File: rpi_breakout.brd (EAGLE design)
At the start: 36.8 x 34.3 mm, 22 parts

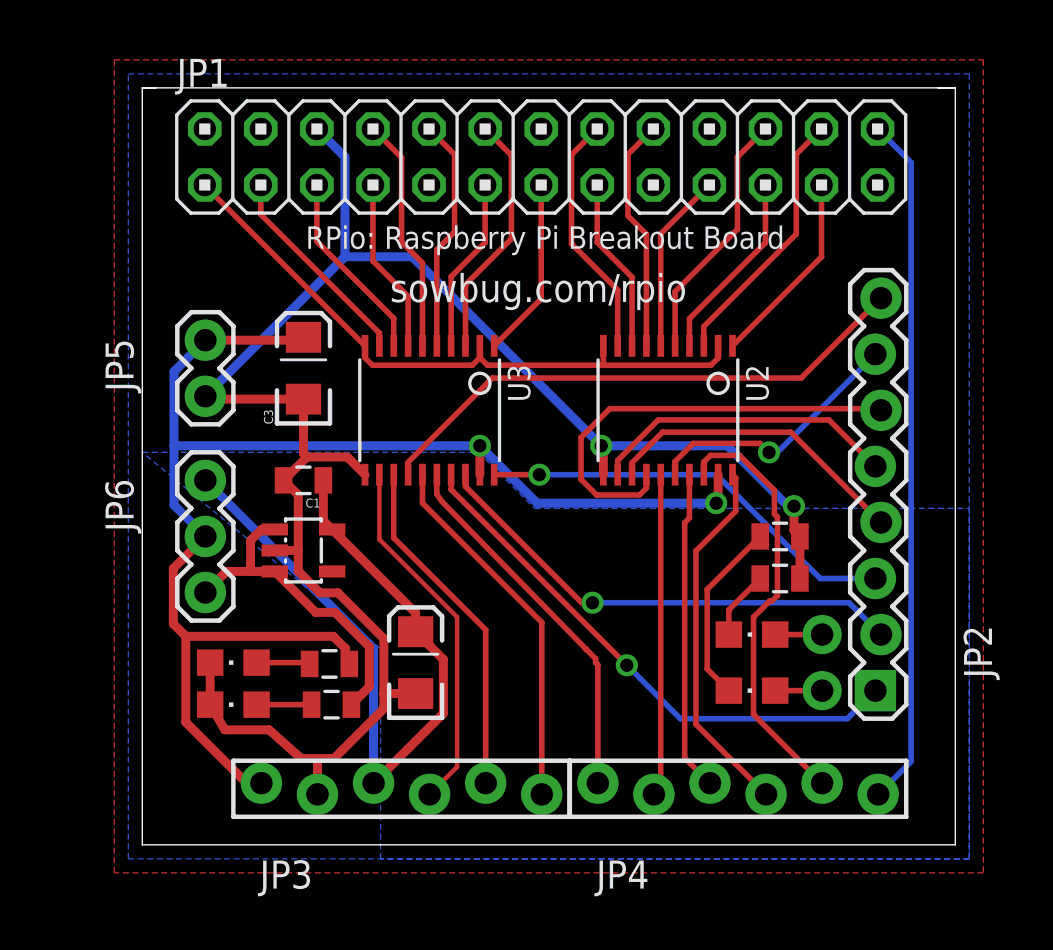
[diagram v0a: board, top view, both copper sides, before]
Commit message: Moved left IC right for shorter traces
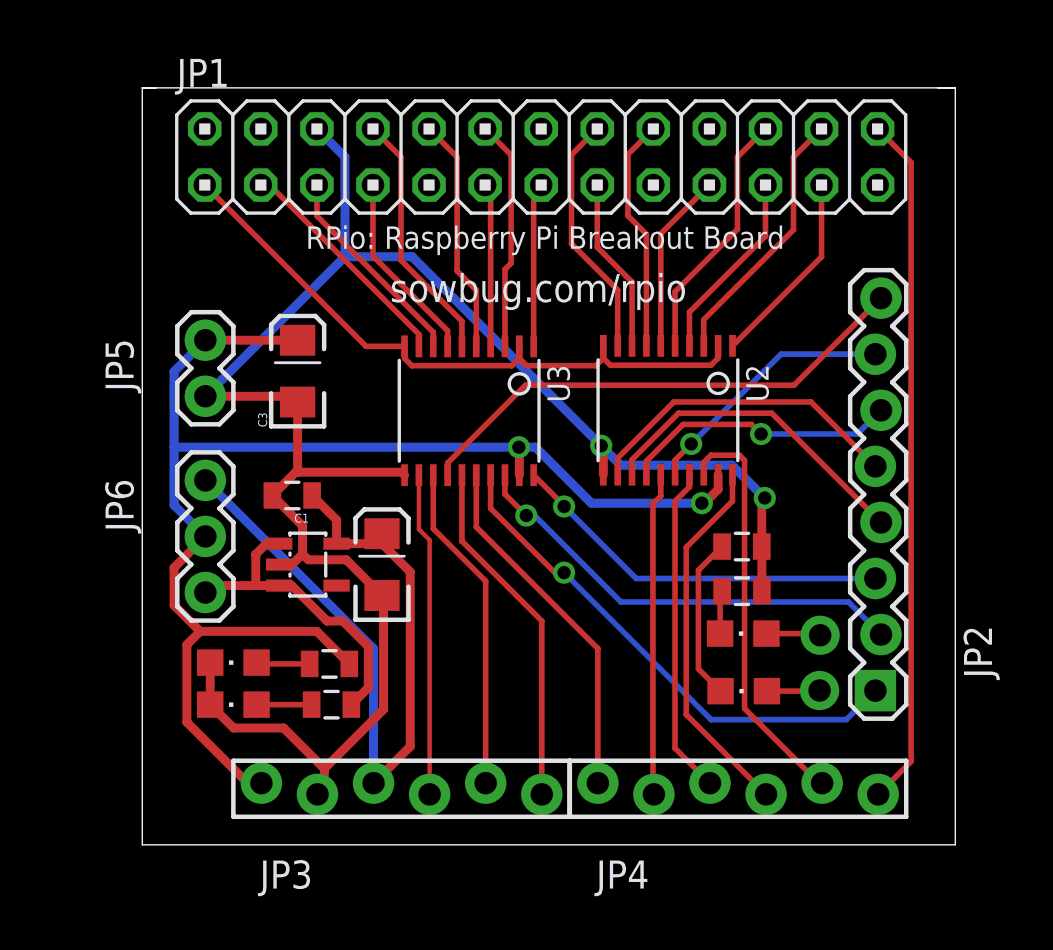
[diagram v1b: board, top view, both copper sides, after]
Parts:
- moved C2 4.69 mm to (10.2, 12.1)
- moved R3 1.82 mm to (26.5, 10.9)
- moved U3 1.79 mm to (14.2, 19.0)
- moved R4 1.79 mm to (26.5, 12.9)
- moved C1 0.85 mm to (6.16, 15.2)
- moved VREG1 0.67 mm to (6.87, 12.1)
- moved LED3 0.40 mm to (26.6, 8.93)
- moved LED4 0.38 mm to (26.6, 6.33)
- moved C3 0.30 mm to (6.40, 20.8)
- moved JP8 0.12 mm to (30.0, 6.36)
- moved JP7 0.09 mm to (30.1, 8.86)
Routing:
- net GPIOV_5: track 20.0 -> 12.6 mm, vias 0 -> 1
- net SDAV0: track 16.5 -> 14.7 mm
- net GPIOV_7: track 25.1 -> 23.3 mm
- net GPIOV_2: track 19.2 -> 17.4 mm
- net GPIOV_1: track 22.1 -> 20.5 mm
- net GPIOV_0: track 24.7 -> 23.4 mm
- net N$3: track 3.13 -> 1.96 mm
- net VCC: track 64.9 -> 63.8 mm
- net SDA0: track 9.51 -> 10.5 mm
- net N$4: track 8.39 -> 7.41 mm
- net /SPI_CEV0: track 19.7 -> 18.8 mm
- net GPIOV_3: track 14.1 -> 14.9 mm
- net TXDV: track 16.7 -> 16.0 mm
- net TXD: track 10.8 -> 11.5 mm
- net SCL0: track 8.73 -> 9.49 mm
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- removed copper zone on layer 1, net GND
- removed copper zone on layer 16, net GND
- removed copper zone on layer 16, net VCC

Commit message: Added solder jumper, RTC and diode protection, shortened traces (26.5 total)
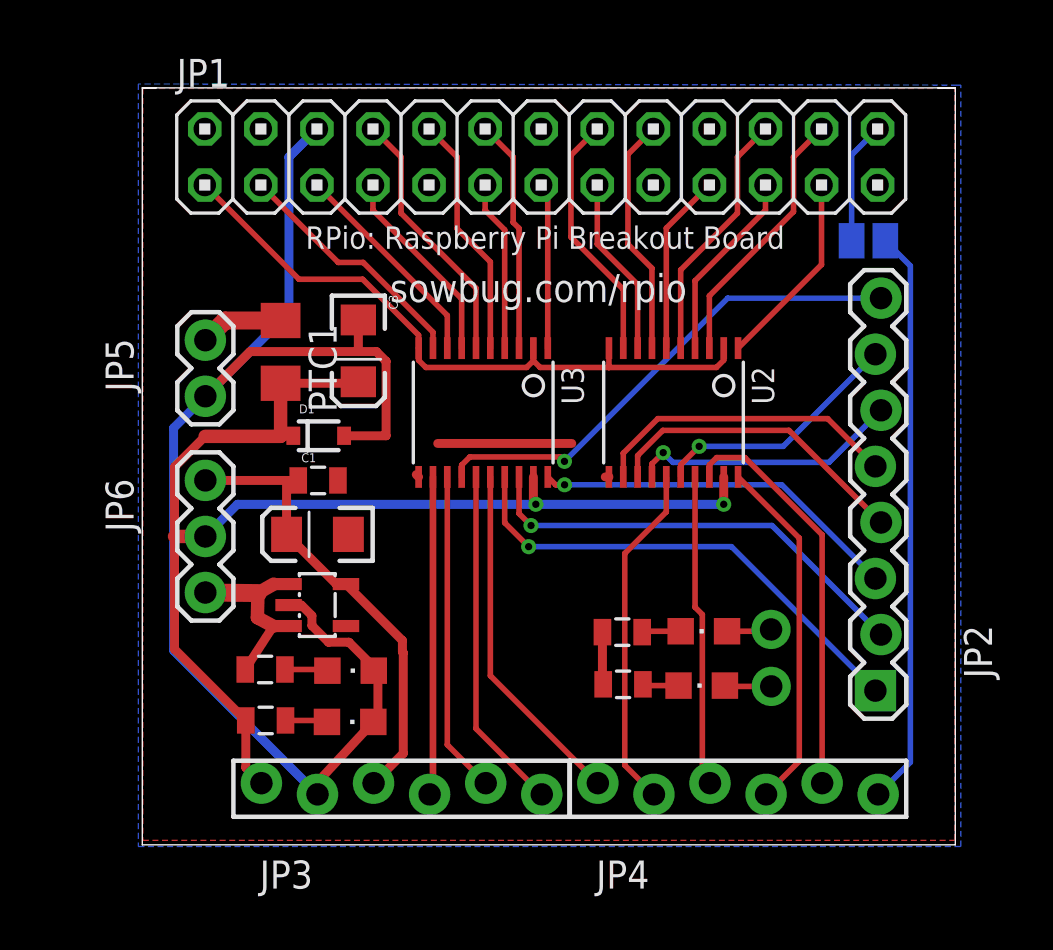
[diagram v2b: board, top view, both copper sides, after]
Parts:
- added D1: (no value), SparkFun-DiscreteSemi:SOD-323
- added PTC1: (no value), rcl:R1206
- added SJ1: SPI_CE1_3.3v_enable, jumper:SJ
- moved R4 8.24 mm to (21.1, 6.64), turned to 180 degrees
- moved LED2 5.93 mm to (8.78, 4.93), turned to 270 degrees
- moved R3 5.73 mm to (21.1, 9.00), turned to 180 degrees
- moved LED1 5.53 mm to (8.80, 7.26), turned to 270 degrees
- moved R2 3.86 mm to (4.95, 5.00), turned to 0 degrees
- moved R1 3.40 mm to (4.93, 7.31), turned to 0 degrees
- moved C2 3.23 mm to (7.30, 13.4), turned to 180 degrees
- moved C3 2.90 mm to (9.15, 21.7), turned to 270 degrees
- moved JP7 2.24 mm to (27.8, 9.12)
- moved JP8 2.20 mm to (27.9, 6.54)
- moved LED4 1.92 mm to (24.7, 6.58)
- moved VREG1 1.88 mm to (7.29, 10.2)
- moved LED3 1.79 mm to (24.8, 9.04)
- moved C1 1.35 mm to (7.33, 15.9), turned to 0 degrees
- moved U3 0.64 mm to (14.8, 18.9)
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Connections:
- new net N$5: JP1.26, SJ1.1
- new net N$6: JP5.1, PTC1.1
- net /SPI_CE1: now also SJ1.2; no longer JP1.26
- net GND: now also D1.2
- net VCC: now also D1.1, PTC1.2; no longer JP5.1
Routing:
- net 3.3V: track 34.1 -> 20.9 mm
- net GND: track 85.8 -> 72.9 mm, vias 2 -> 0
- net VCC: track 63.8 -> 55.9 mm
- net N$4: track 7.41 -> 1.64 mm
- net N$5: track 0.00 -> 5.55 mm
- net 5V: track 14.3 -> 8.84 mm
- net /SPI_CE1: track 31.4 -> 26.2 mm
- net N$6: track 0.00 -> 3.78 mm
- net GPIOV_0: track 23.4 -> 22.0 mm
- net SPI_MOSIV: track 14.7 -> 15.7 mm
- net SDA0: track 10.5 -> 11.3 mm
- net SPI_MISOV: track 14.9 -> 14.2 mm
- net SPI_SCLKV: track 16.8 -> 16.2 mm
- net GPIOV_2: track 17.4 -> 16.7 mm
- net GPIOV_3: track 14.9 -> 14.2 mm
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- added copper zone on layer 1, net GND
- added copper zone on layer 16, net GND

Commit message: SCL/SDA pullup, 4.7K. GPIO labels are back.
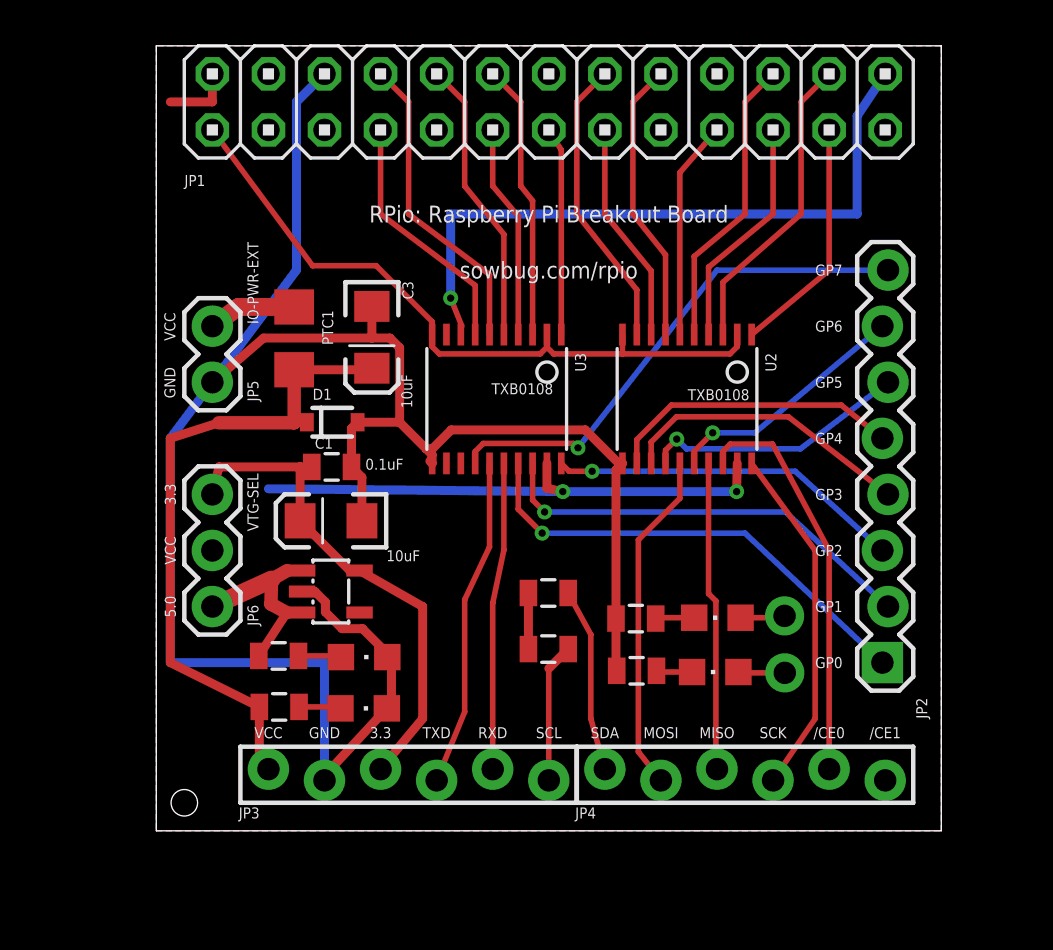
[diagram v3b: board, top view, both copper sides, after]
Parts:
- removed SJ1: SPI_CE1_3.3v_enable, jumper:SJ
- added R5, R6: 4K7, SparkFun:0805
- JP3: value (none) -> SHIFT2
- JP4: value (none) -> SHIFT1
- JP7: value (none) -> LED3
- JP8: value (none) -> LED4
- U2, U3: value (none) -> TXB0108
- moved JP1 2.52 mm to (17.8, 33.0)
- moved JP2 1.31 mm to (33.0, 7.62)
- moved JP7 0.87 mm to (28.5, 9.74)
- moved C1 0.87 mm to (7.94, 16.5)
- moved LED1 0.87 mm to (9.41, 7.87)
- moved LED2 0.87 mm to (9.39, 5.55)
- moved R2 0.87 mm to (5.57, 5.61)
- moved C2 0.87 mm to (7.92, 14.0)
- moved D1 0.87 mm to (7.97, 18.5)
- moved PTC1 0.87 mm to (6.25, 22.3)
- moved R1 0.87 mm to (5.54, 7.92)
- moved VREG1 0.87 mm to (7.91, 10.8)
- moved C3 0.87 mm to (9.77, 22.4)
- moved JP8 0.87 mm to (28.5, 7.16)
- moved LED3 0.87 mm to (25.4, 9.65)
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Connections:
- net N$6 renamed VCC_FUSE
- removed net 5V0: JP1.2
- removed net N$5: JP1.26, SJ1.1
- removed net SCLV0: JP3.5, U3.13
- removed net SDAV0: JP3.4, U3.12
- new net /SPI_CEV1: JP4.6, U3.13
- net /SPI_CE1: now also JP1.26, U3.8; no longer JP4.6, SJ1.2
- net 3V3_RPI: now also R5.1, R6.1
- net 5V: now also JP1.2
- net RXDV: now also JP3.5; no longer JP4.1
- net SCL0: now also JP3.6, R6.2; no longer U3.8
- net SDA0: now also JP4.1, R5.2; no longer U3.9
- net TXDV: now also JP3.4; no longer JP3.6
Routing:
- net GND: track 72.9 -> 97.1 mm
- net SCLV0: track 14.6 -> 0.00 mm
- net SDAV0: track 14.4 -> 0.00 mm
- net N$5: track 5.55 -> 0.00 mm
- net /SPI_CE1: track 26.2 -> 30.3 mm, vias 0 -> 1
- net 3V3_RPI: track 30.0 -> 34.1 mm
- net SCL0: track 9.83 -> 6.31 mm
- net 5V: track 8.84 -> 11.9 mm
- net SDA0: track 11.3 -> 8.33 mm
- net GPIO_7: track 9.05 -> 11.4 mm
- net TXD: track 11.9 -> 14.2 mm
- net GPIO_5: track 10.9 -> 12.9 mm
- net RXDV: track 15.9 -> 13.9 mm
- net 3.3V: track 20.9 -> 22.9 mm
- net SPI_SCLK: track 8.95 -> 10.9 mm
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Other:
- board size 36.8 x 34.3 mm -> 35.6 x 35.6 mm
- board text added: "/CE0"
- board text added: "/CE1"
- board text added: "3.3"
- board text added: "5.0"
- board text added: "GND"
- board text added: "GP0"
- board text added: "GP1"
- board text added: "GP2"
- board text added: "GP3"
- board text added: "GP4"
- board text added: "GP5"
- board text added: "GP6"
- board text added: "GP7"
- board text added: "MISO"
- board text added: "MOSI"
- board text added: "RXD"
- board text added: "SCK"
- board text added: "SCL"
- board text added: "SDA"
- board text added: "TXD"
- board text added: "VCC"

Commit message: Moved pullup resistors near power.
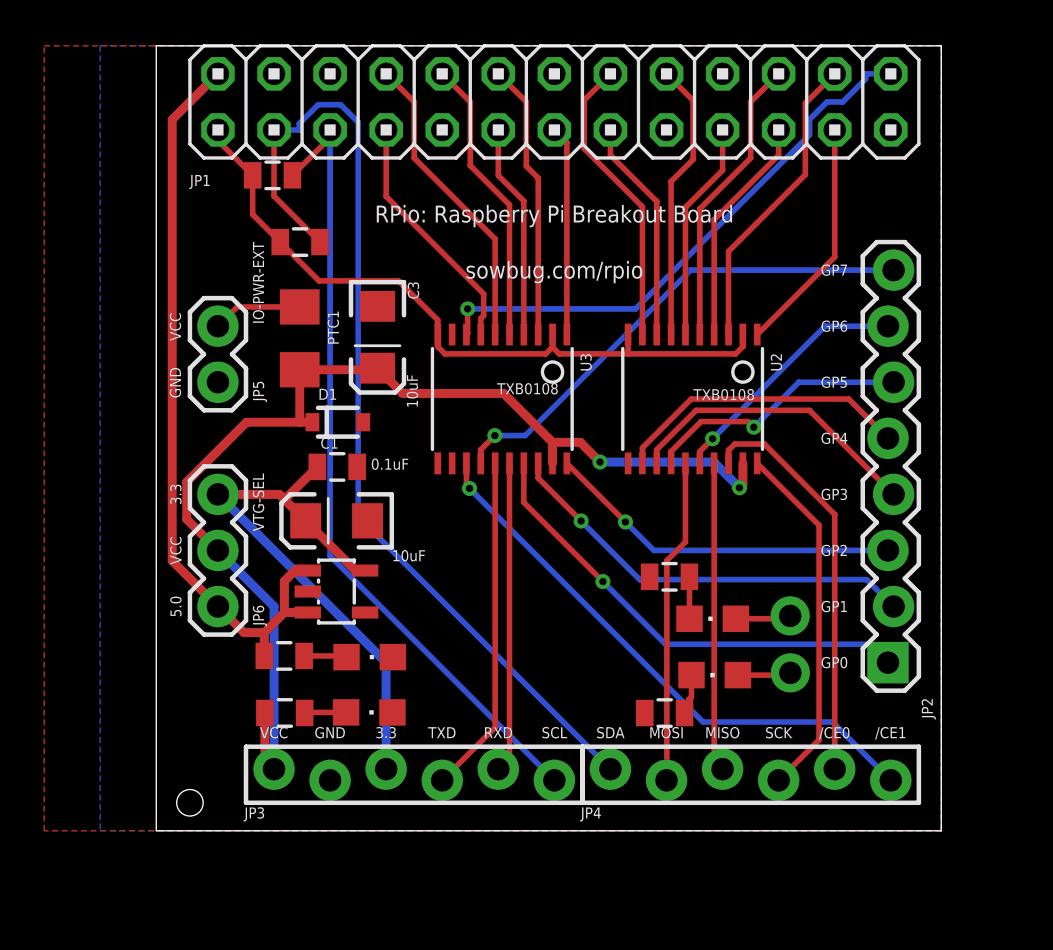
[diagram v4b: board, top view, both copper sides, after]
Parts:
- moved R6 24.8 mm to (5.27, 29.7)
- moved R5 19.5 mm to (6.51, 26.7)
- moved R3 2.43 mm to (23.3, 11.5)
- moved R4 2.30 mm to (23.0, 5.33)
- moved R2 0.37 mm to (5.82, 5.34)
- moved LED2 0.31 mm to (9.65, 5.36)
- moved C3 0.25 mm to (10.0, 22.4)
- moved JP8 0.25 mm to (28.7, 7.16)
- moved U2 0.25 mm to (24.3, 19.6)
- moved U3 0.25 mm to (15.7, 19.6)
- moved C2 0.25 mm to (8.17, 14.0)
- moved PTC1 0.25 mm to (6.50, 22.3)
- moved R1 0.25 mm to (5.80, 7.92)
- moved C1 0.25 mm to (8.20, 16.5)
- moved D1 0.25 mm to (8.22, 18.5)
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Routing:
- net GND: track 97.1 -> 0.00 mm
- net SDA0: track 8.33 -> 44.8 mm
- net SCL0: track 6.31 -> 36.4 mm
- net /SPI_CEV1: track 0.00 -> 25.8 mm, vias 0 -> 1
- net 5V: track 11.9 -> 34.5 mm
- net /SPI_CE1: track 30.3 -> 25.3 mm
- net VCC: track 54.2 -> 50.9 mm
- net 3.3V: track 22.9 -> 25.8 mm
- net 3V3_RPI: track 34.1 -> 32.4 mm
- net SPI_MOSIV: track 15.5 -> 14.7 mm
- net GPIOV_7: track 23.4 -> 22.7 mm
- net N$3: track 1.76 -> 2.32 mm
